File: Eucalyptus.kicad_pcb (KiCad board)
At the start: 2 copper layers, 60 x 35 mm, 65 parts, among them J1 HEADER_2, J10 ICSP, J11 HEADER_1, J12 HEADER_1, J13 HEADER_1, J14 HEADER_1, J15 HEADER_1, J16 motores, J17 motores, J18 HEADER_1, J19 HEADER_1, J2 Transmisor RF, J20 HEADER_1, J21 HEADER_1, J22 HEADER_1, J23 HEADER_1, J24 HEADER_2, J3 HEADER_1, J4 HEADER_1, J5 HEADER_1, J6 HEADER_1, J7 HEADER_1, J8 HEADER_1, J9 HEADER_1, Q1 2N7002, SW2 SW_PUSH, SW3 Estrategias, U1 LM1117-SOT, U2 ATMEGA328P-AU, U3 DRV8872, U4 DRV8872, Y2 Crystal_GND23_Small

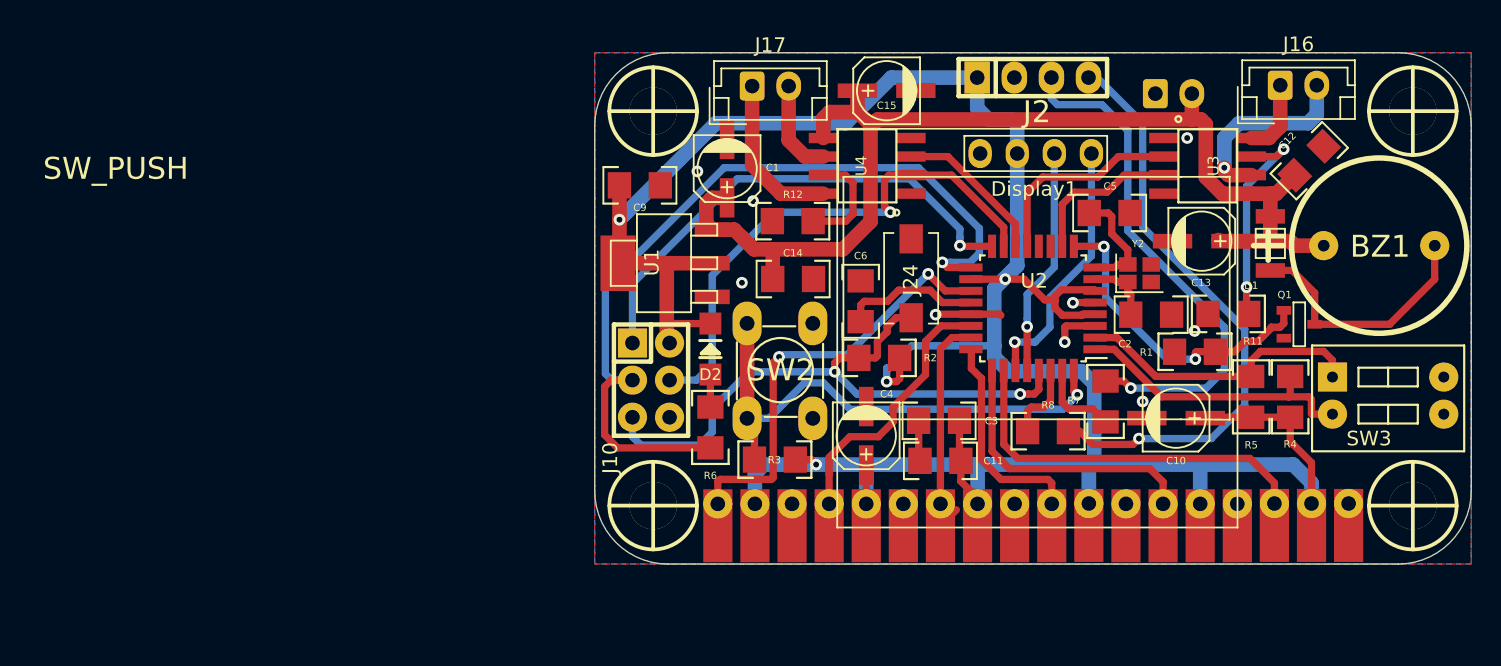
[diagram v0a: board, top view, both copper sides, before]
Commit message: MODIFICACIONES
SE MODIFICO PCB,SERIGRAFIA Y ARCHIVOS GERBERS
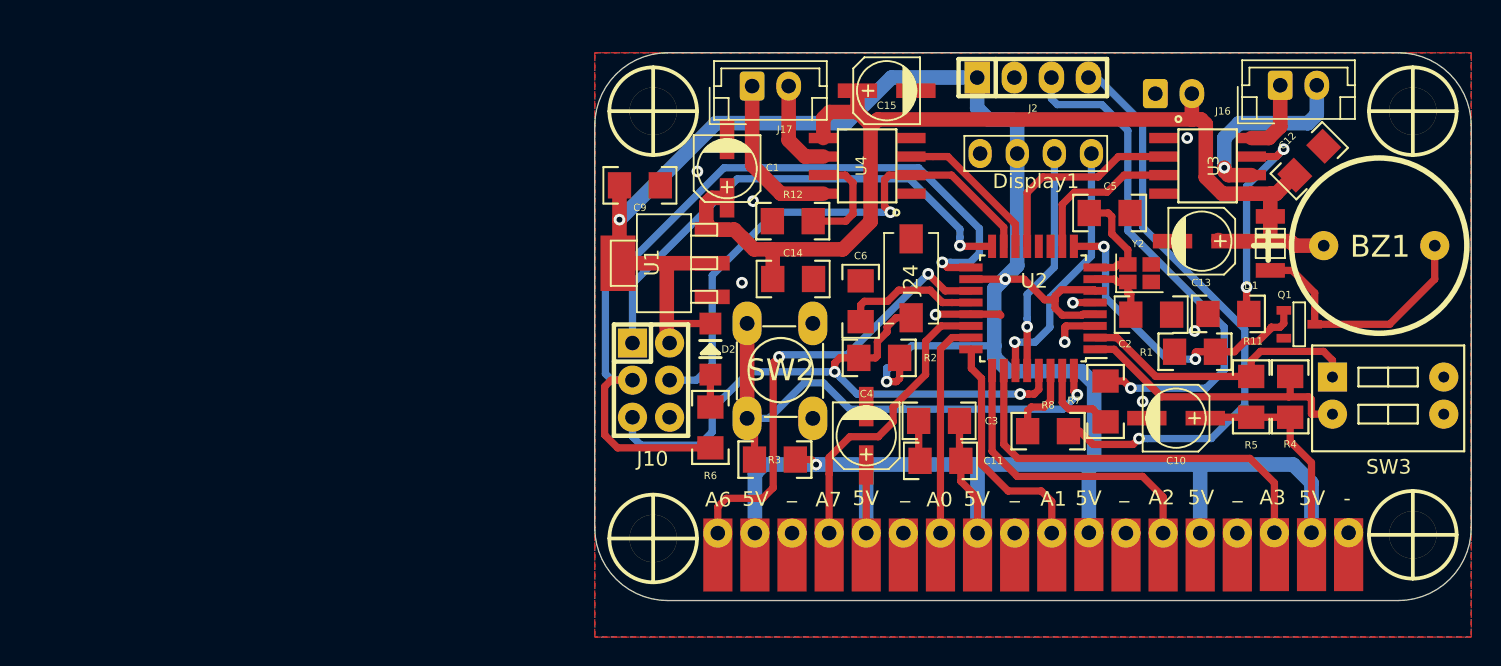
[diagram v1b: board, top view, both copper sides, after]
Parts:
- removed G***: LOGO, logo:c
- removed G***: LOGO, logo:log02
- Display1: footprint EESTN5:128x64OLED -> Eucalyptus:128x64OLED
- J1: value HEADER_2 -> BATERIA
- moved H3 2.25 mm to (94.0, 128.2)
- moved H1 2.00 mm to (146.0, 128.0)
- moved J11 2.00 mm to (116.2, 129.4)
- moved J12 2.00 mm to (128.9, 129.4)
- moved J13 2.00 mm to (126.4, 129.4)
- moved J14 2.00 mm to (123.8, 129.4)
- moved J15 2.00 mm to (121.3, 129.4)
- moved J18 2.00 mm to (103.5, 129.4)
- moved J19 2.00 mm to (101.0, 129.4)
- moved J20 2.00 mm to (98.4, 129.4)
- moved J21 2.00 mm to (111.1, 129.4)
- moved J22 2.00 mm to (108.6, 129.4)
- moved J23 2.00 mm to (106.0, 129.4)
- moved J3 2.00 mm to (141.6, 129.4)
- moved J4 2.00 mm to (139.1, 129.4)
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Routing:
- net +5V: track 189.2 -> 201.0 mm
- net /DISTANCIA_D: track 26.1 -> 29.6 mm
- net /DISTANCIA_FD: track 21.1 -> 20.5 mm
- net /TATAMI_TI: track 31.3 -> 30.7 mm
- net /DISTANCIA_FI: track 16.3 -> 15.7 mm
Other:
- board size 60 x 35 mm -> 60 x 37.5 mm
- board text added: "-"
- board text added: "5V"
- board text added: "A0"
- board text added: "A1"
- board text added: "A2"
- board text added: "A3"
- board text added: "A6"
- board text added: "A7"
- board text added: "_"

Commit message: modificaciones
se agrego logos
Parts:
- added G***: LOGO, logo:log02, B.Cu at (96.5, 107.6)
- added G***: LOGO, logo:c, B.Cu at (113.3, 120.2)
- added G***: LOGO, logo:jj, B.Cu at (132.6, 122.7)
- added G***: LOGO, logo:b, B.Cu at (105.6, 103.7)
